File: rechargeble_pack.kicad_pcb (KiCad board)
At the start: 2 copper layers, 67 x 32.5 mm, 42 parts, among them J1 Out, J2 LiPo, J3 DC IN, Q1 SIA453, Q2 BC857, Q6 BC847, Q7 BC857, U1 TP4056, U2 TPS61041

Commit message: need fix
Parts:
- moved D1 65.7 mm to (83.6, 26.4)
- moved C8 41.2 mm to (85.5, 31.0), turned to 0 degrees
- moved C7 39.6 mm to (47.5, 4.00), turned to 90 degrees
- moved Q7 27.8 mm to (55.0, -8.50)
- moved R3 26.2 mm to (54.0, 19.0), turned to 0 degrees
- moved C3 26.2 mm to (59.5, 28.5)
- moved Q6 23.0 mm to (47.1, 23.0)
- moved R8 21.1 mm to (37.0, 37.5), turned to 0 degrees
- moved C4 19.0 mm to (54.0, 23.5), turned to 0 degrees
- moved R2 18.4 mm to (59.5, 23.5), turned to 0 degrees
- moved R9 16.3 mm to (15.5, 27.6), turned to 90 degrees
- moved C9 15.9 mm to (56.0, 37.0), turned to 0 degrees
- moved L2 14.4 mm to (51.0, 41.5), turned to 180 degrees
- moved C14 12.7 mm to (22.6, 22.0)
- moved U2 12.5 mm to (41.0, 12.9), turned to 90 degrees
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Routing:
- net GND: track 197.8 -> 0.00 mm, vias 2 -> 0
- net VCC: track 83.3 -> 0.00 mm, vias 4 -> 0
- net Net-(D1-A): track 65.2 -> 0.00 mm, vias 2 -> 0
- net +9V: track 64.1 -> 0.00 mm, vias 3 -> 0
- net VBUS: track 47.6 -> 0.00 mm
- net Net-(Q6-B): track 45.6 -> 0.00 mm, vias 4 -> 0
- net +10V: track 40.4 -> 0.00 mm, vias 3 -> 0
- net Net-(Q7-B): track 40.1 -> 0.00 mm, vias 2 -> 0
- net +BATT: track 37.1 -> 0.00 mm
- net Net-(U2-FB): track 33.4 -> 0.00 mm, vias 2 -> 0
- net Net-(D2-K): track 30.8 -> 0.00 mm, vias 2 -> 0
- net /OUT_EN: track 30.2 -> 0.00 mm
- net Net-(D1-K): track 28.3 -> 0.00 mm, vias 2 -> 0
- net Net-(Q2-C): track 26.3 -> 0.00 mm, vias 2 -> 0
- net Net-(U1-PROG): track 19.8 -> 0.00 mm, vias 2 -> 0
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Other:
- board size 67 x 32.5 mm -> 70 x 32.5 mm

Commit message: final
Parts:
- moved C8 57.1 mm to (28.5, 28.5), turned to -90 degrees
- moved R8 32.9 mm to (55.0, 10.0), turned to -90 degrees
- moved Q2 30.9 mm to (59.5, 4.00), turned to 90 degrees
- moved D1 29.1 mm to (65.0, 4.00), turned to 90 degrees
- moved C10 26.4 mm to (59.5, 9.50), turned to 0 degrees
- moved R4 25.3 mm to (49.0, 13.5)
- moved Q7 25.3 mm to (42.4, 13.5)
- moved R6 24.5 mm to (49.5, 5.09), turned to -90 degrees
- moved R7 21.8 mm to (55.0, 6.09), turned to -90 degrees
- moved C9 21.1 mm to (54.5, 15.9), turned to -90 degrees
- moved C7 18.3 mm to (65.0, 9.50), turned to -90 degrees
- moved R5 17.5 mm to (49.5, 19.5), turned to 0 degrees
- moved D4 17.4 mm to (8.50, 10.6), turned to -90 degrees
- moved L2 16.6 mm to (49.5, 25.0)
- moved C11 12.4 mm to (60.0, 15.9), turned to -90 degrees
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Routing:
- net GND: track 0.00 -> 204.1 mm, vias 0 -> 2
- net VCC: track 0.00 -> 77.6 mm
- net VBUS: track 0.00 -> 66.4 mm
- net Net-(D1-A): track 0.00 -> 53.9 mm, vias 0 -> 3
- net +10V: track 0.00 -> 43.9 mm, vias 0 -> 2
- net Net-(U2-FB): track 0.00 -> 38.6 mm, vias 0 -> 2
- net Net-(Q2-C): track 0.00 -> 36.1 mm, vias 0 -> 4
- net +BATT: track 0.00 -> 35.7 mm
- net +9V: track 0.00 -> 31.8 mm, vias 0 -> 1
- net Net-(U1-PROG): track 0.00 -> 27.0 mm, vias 0 -> 2
- net Net-(D2-K): track 0.00 -> 26.4 mm, vias 0 -> 2
- net Net-(Q6-B): track 0.00 -> 20.6 mm
- net /OUT_EN: track 0.00 -> 15.5 mm
- net Net-(D3-K): track 0.00 -> 13.1 mm
- net Net-(Q7-B): track 0.00 -> 11.1 mm
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
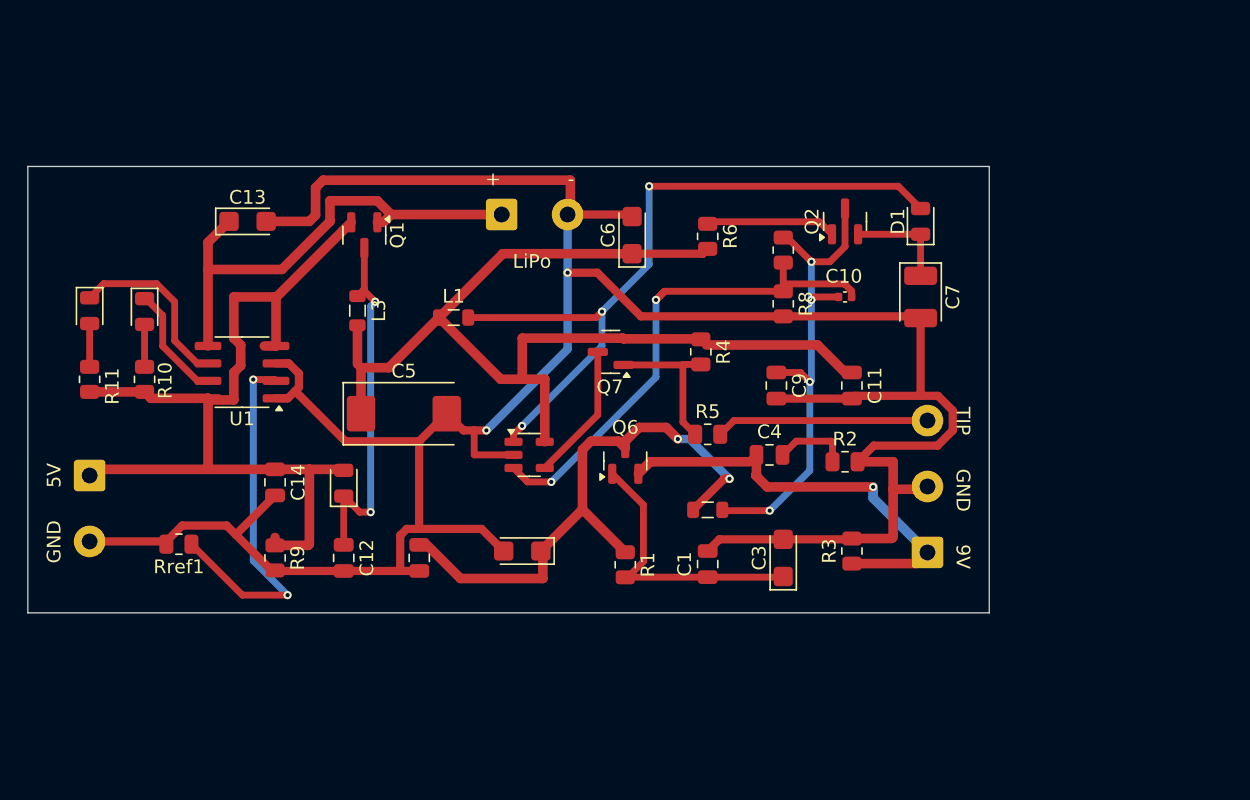
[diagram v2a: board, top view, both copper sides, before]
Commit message: fix mosfet
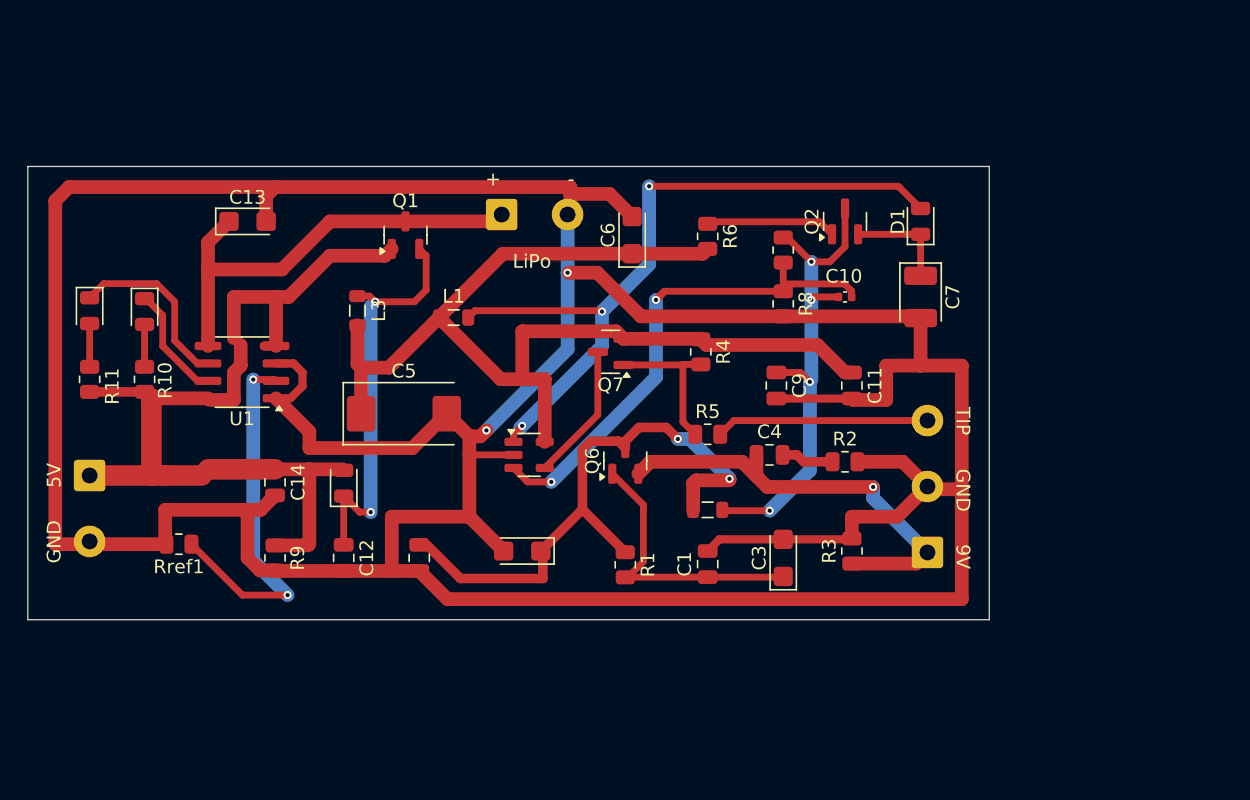
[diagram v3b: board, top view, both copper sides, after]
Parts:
- Q1: value SIA453 -> IRLML6402
- moved Q1 3.00 mm to (27.5, 5.00), turned to 90 degrees
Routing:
- net GND: track 204.1 -> 305.9 mm
- net Net-(D2-K): track 26.4 -> 30.2 mm
- net VBUS: track 66.4 -> 68.9 mm
- net +BATT: track 35.7 -> 33.4 mm
- net Net-(C4-Pad2): track 5.50 -> 3.84 mm
- net VCC: track 77.6 -> 78.3 mm
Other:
- board size 70 x 32.5 mm -> 70 x 33 mm

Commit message: gnd polygon
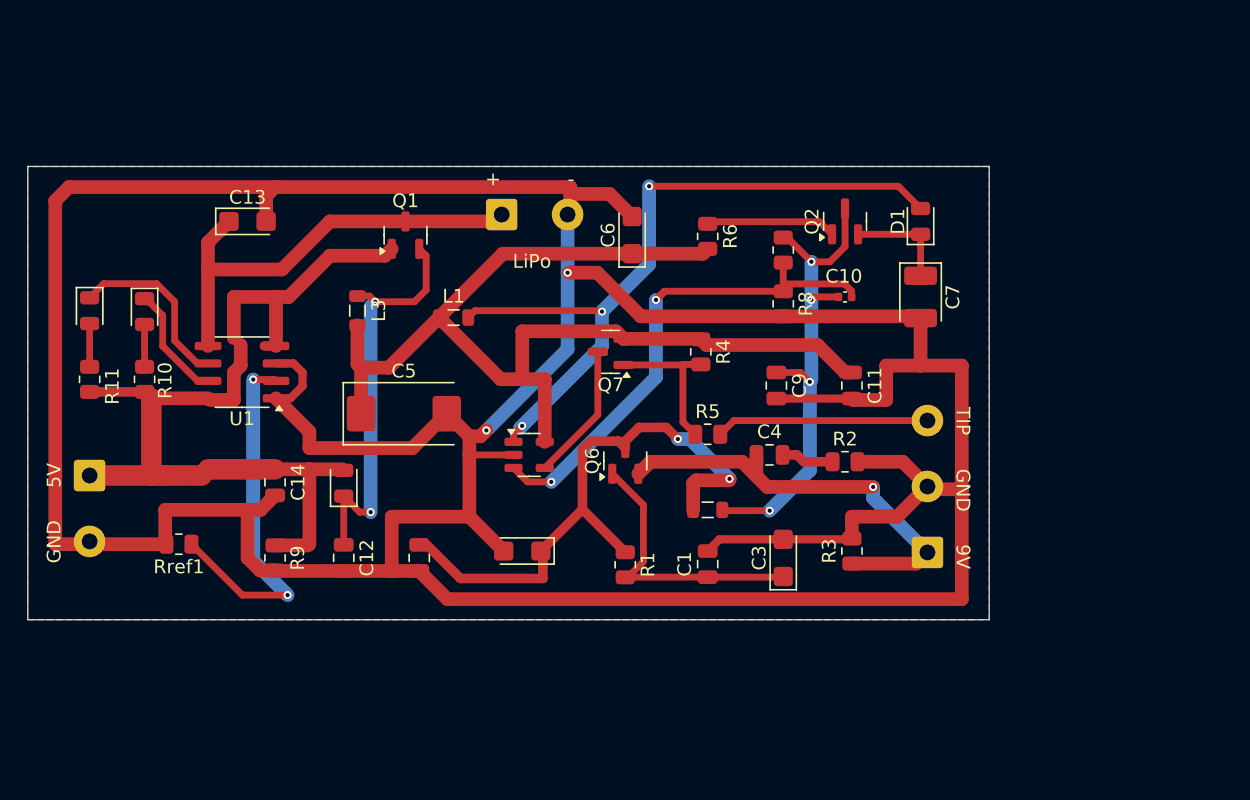
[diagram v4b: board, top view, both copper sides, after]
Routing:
- added copper zone on B.Cu, net GND
- added copper zone on F.Cu, net GND
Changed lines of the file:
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@@
 		(net 22)
+	)
+	(zone
+		(net 1)
+		(net_name "GND")
+		(layers "F.Cu" "B.Cu")
+		(hatch edge 0.5)
+		(connect_pads
+			(clearance 0.5)
+		)
+		(min_thickness 0.25)
+		(filled_areas_thickness no)
+		(fill yes
+			(thermal_gap 0.5)
+			(thermal_bridge_width 0.5)
+		)
+		(polygon
+			(pts
+				(xy 0 0) (xy 0 33) (xy 70 33) (xy 70 0)
+			)
+		)
 	)
 	(embedded_fonts no)
